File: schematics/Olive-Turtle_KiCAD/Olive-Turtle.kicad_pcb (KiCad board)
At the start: 2 copper layers, 10 parts, among them IC1 ENS160-BGLT, U1 ESP32-DEVKITC-32U

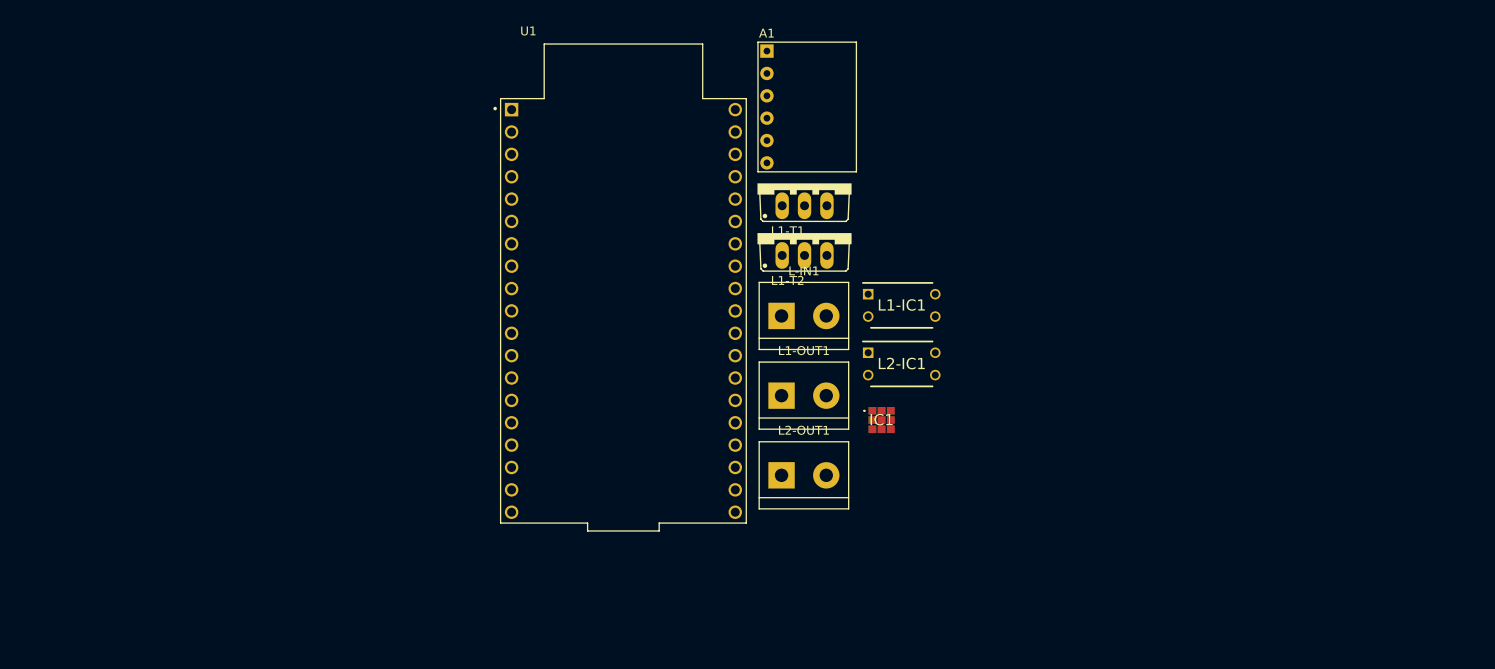
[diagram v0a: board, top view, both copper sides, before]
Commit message: [develop] Schematic for LC
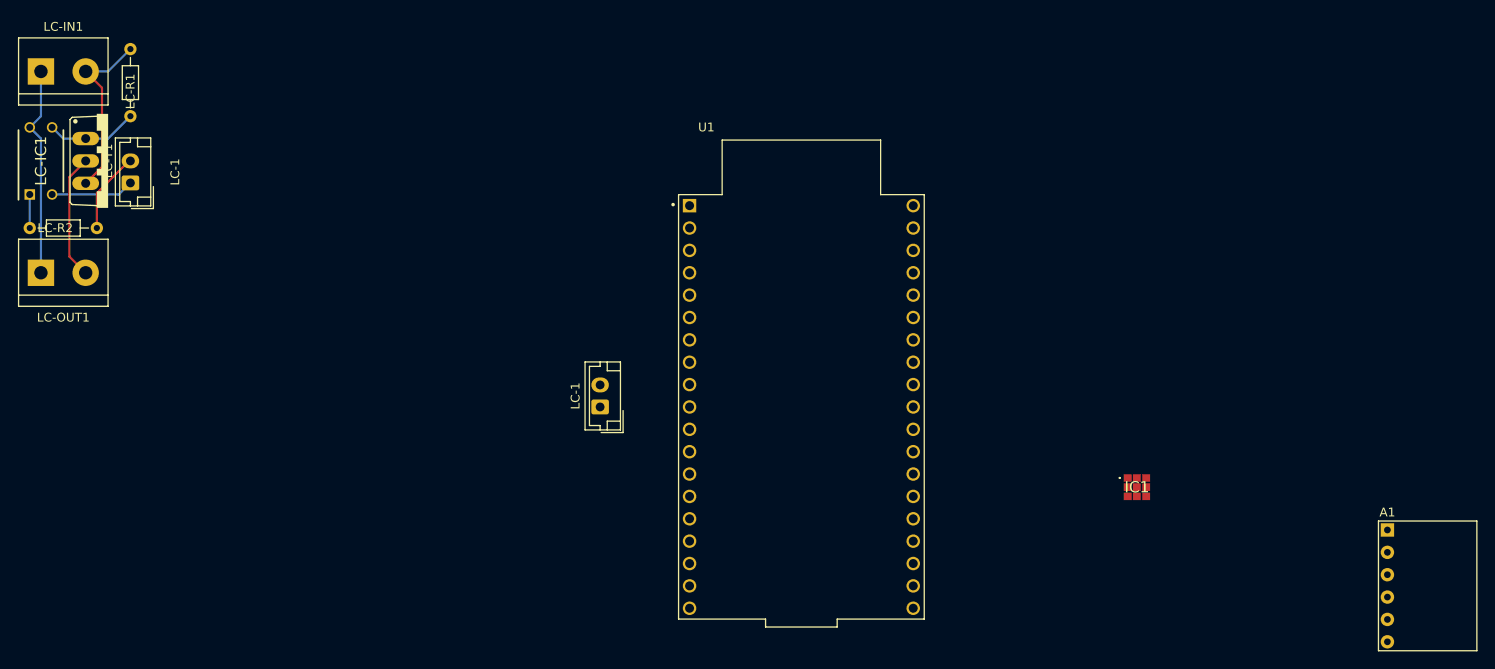
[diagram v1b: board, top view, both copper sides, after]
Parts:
- removed L-IN1, L1-OUT1, L2-OUT1: Screw_Terminal_01x02, TerminalBlock:TerminalBlock_bornier-2_P5.08mm
- removed L1-IC1, L2-IC1: TLP621, TLP621:DIP762W60P254L460H450Q4N
- removed L1-T1, L1-T2: IRF520, IRF520:TO220BV
- added LC-1: JST 2.5mm 2P Wafer, Connector_JST:JST_EH_B2B-EH-A_1x02_P2.50mm_Vertical, F.Cu at (63.5, 68.5)
- added LC-1: JST 2.5mm 2P Wafer, Connector_JST:JST_EH_B2B-EH-A_1x02_P2.50mm_Vertical, F.Cu at (116.8, 94.0)
- added LC-IC1: TLP621, TLP621:DIP762W60P254L460H450Q4N, F.Cu at (53.3, 66.0)
- added LC-IN1: Screw_Terminal_01x02, TerminalBlock:TerminalBlock_bornier-2_P5.08mm, F.Cu at (53.3, 55.9)
- added LC-OUT1: Screw_Terminal_01x02, TerminalBlock:TerminalBlock_bornier-2_P5.08mm, F.Cu at (53.3, 78.7)
- added LC-R1: 2.2k R, Resistor_THT:R_Axial_DIN0204_L3.6mm_D1.6mm_P7.62mm_Horizontal, F.Cu at (63.5, 53.3)
- added LC-R2: 330 R, Resistor_THT:R_Axial_DIN0204_L3.6mm_D1.6mm_P7.62mm_Horizontal, F.Cu at (52.1, 73.7)
- added LC-T1: IRF520, IRF520:TO220BV, F.Cu at (61.0, 66.0)
- moved A1 89.0 mm to (206.2, 108.0)
- moved IC1 30.0 mm to (177.8, 103.1)
- moved U1 23.0 mm to (139.7, 94.0)
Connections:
- U1 pad 14: Net-(L1-IC1-K) -> /LC1-G
- U1 pad 5: Net-(U1-IO34) -> unconnected-(U1-IO34-Pad5)
- U1 pad 6: Net-(U1-IO35) -> /LC1-S
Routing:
- net /LED Control/12V: track 0.00 -> 25.7 mm
- net /LED Control/GND: track 0.00 -> 20.4 mm
- net Net-(LC-OUT1-Pin_2): track 0.00 -> 14.2 mm
- net Net-(LC-IC1-E): track 0.00 -> 10.5 mm
- net /LED Control/LC-G: track 0.00 -> 9.43 mm
- net /LED Control/LC-S: track 0.00 -> 9.29 mm
- net Net-(LC-IC1-A): track 0.00 -> 3.81 mm
